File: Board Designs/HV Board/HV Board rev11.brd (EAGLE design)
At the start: 119.1 x 71.4 mm, 73 parts, among them IC1 OKI-78SR-5, IC2 NE5532SOIC

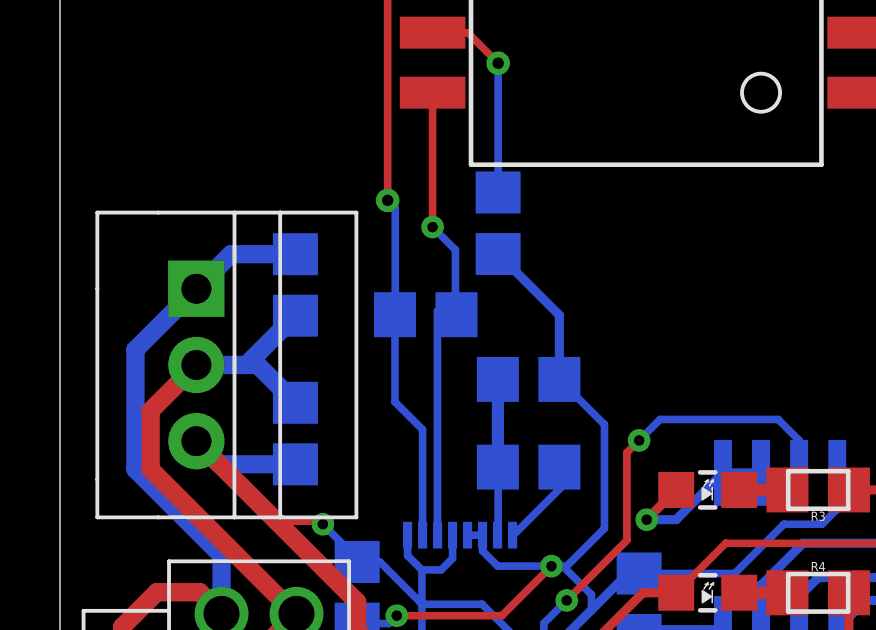
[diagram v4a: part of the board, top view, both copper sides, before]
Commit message: HV Board rev11: comp hardware - removed extra isoSPI resistor, changed LED resistor value
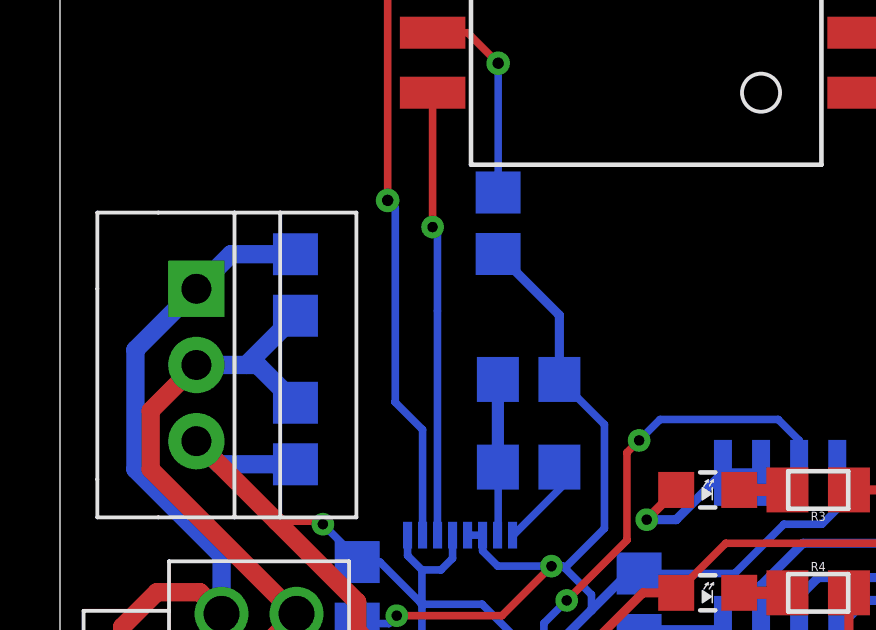
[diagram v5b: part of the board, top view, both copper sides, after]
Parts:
- removed R35: 120, HyTechDevices:0805
- R4: value 5k -> 2k
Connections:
- net IM: no longer R35.1
- net IP: no longer R35.2
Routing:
- net IP: track 15.9 -> 14.8 mm
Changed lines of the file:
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@@
 <layer number="18" name="Vias" color="2" fill="1" visible="yes" active="yes"/>
 <layer number="19" name="Unrouted" color="6" fill="1" visible="yes" active="yes"/>
-<layer number="20" name="Dimension" color="15" fill="1" visible="yes" active="yes"/>
+<layer number="20" name="Dimension" color="14" fill="1" visible="yes" active="yes"/>
 <layer number="21" name="tPlace" color="7" fill="1" visible="yes" active="yes"/>
 <layer number="22" name="bPlace" color="7" fill="1" visible="yes" active="yes"/>
@@
 <circle x="6.4008" y="23.6728" radius="3" width="0.127" layer="40"/>
 <circle x="32.3088" y="50.3428" radius="3" width="0.127" layer="40"/>
+<dimension x1="0" y1="71.374" x2="119.126" y2="71.374" x3="59.563" y3="73.406" textsize="1.778" layer="20"/>
+<dimension x1="0" y1="0" x2="0" y2="71.374" x3="-2.286" y3="35.687" textsize="1.778" layer="20"/>
 </plain>
 <attributes>
@@
 <attribute name="VALUE" x="28.702" y="45.4152" size="0.889" layer="27" font="vector" rot="R180" align="center"/>
 </element>
-<element name="R4" library="HyTechDevices" package="0805" value="5k" x="25.273" y="42.037" smashed="yes">
+<element name="R4" library="HyTechDevices" package="0805" value="2k" x="25.273" y="42.037" smashed="yes">
 <attribute name="NAME" x="25.273" y="42.7609" size="0.3048" layer="25" align="bottom-center"/>
 <attribute name="VALUE" x="28.194" y="42.0878" size="0.889" layer="27" font="vector" align="center"/>
@@
 <attribute name="VALUE" x="15.621" y="50.6222" size="0.889" layer="28" font="vector" rot="MR180" align="center"/>
 </element>
-<element name="R35" library="HyTechDevices" package="0805" value="120" x="12.192" y="51.308" smashed="yes" rot="MR180">
-<attribute name="NAME" x="12.192" y="50.5841" size="0.3048" layer="26" rot="MR180" align="bottom-center"/>
-<attribute name="VALUE" x="12.192" y="52.7812" size="0.889" layer="28" font="vector" rot="MR180" align="center"/>
-</element>
 <element name="C4" library="HyTechDevices" package="0805" value="27pF" x="14.605" y="54.356" smashed="yes" rot="MR270">
 <attribute name="NAME" x="14.3891" y="53.848" size="0.3048" layer="26" rot="MR270" align="bottom-center"/>
@@
 <signal name="IM">
 <contactref element="U$8" pad="10"/>
-<contactref element="R35" pad="1"/>
 <contactref element="U$2" pad="P$10"/>
 <wire x1="10.922" y1="62.357" x2="10.922" y2="55.118" width="0.254" layer="1"/>
-<wire x1="11.176" y1="54.864" x2="11.176" y2="51.317" width="0.254" layer="16"/>
-<wire x1="11.167" y1="51.308" x2="11.176" y2="51.317" width="0.254" layer="16"/>
-<wire x1="11.176" y1="54.864" x2="10.922" y2="55.118" width="0.254" layer="16"/>
+<wire x1="10.922" y1="55.118" x2="11.176" y2="54.864" width="0.254" layer="16"/>
 <via x="10.922" y="55.118" extent="1-16" drill="0.381"/>
 <wire x1="12.42" y1="62.707" x2="11.272" y2="62.707" width="0.254" layer="1"/>
 <wire x1="11.272" y1="62.707" x2="10.922" y2="62.357" width="0.254" layer="1"/>
-<wire x1="12.086" y1="47.477" x2="11.167" y2="48.396" width="0.254" layer="16"/>
-<wire x1="11.167" y1="51.308" x2="11.167" y2="48.396" width="0.254" layer="16"/>
+<wire x1="11.167" y1="48.396" x2="12.086" y2="47.477" width="0.254" layer="16"/>
 <wire x1="12.086" y1="47.477" x2="12.086" y2="43.959" width="0.254" layer="16"/>
+<wire x1="11.176" y1="48.405" x2="11.167" y2="48.396" width="0.254" layer="16"/>
+<wire x1="11.176" y1="54.864" x2="11.176" y2="48.405" width="0.254" layer="16"/>
 </signal>
 <signal name="IP">
 <contactref element="U$8" pad="11"/>
-<contactref element="R35" pad="2"/>
 <contactref element="U$2" pad="P$12"/>
-<wire x1="13.217" y1="51.308" x2="13.182" y2="51.308" width="0.254" layer="16"/>
 <via x="12.42" y="54.229" extent="1-16" drill="0.35"/>
 <wire x1="12.42" y1="58.707" x2="12.42" y2="54.229" width="0.254" layer="1"/>
-<wire x1="12.42" y1="54.229" x2="13.182" y2="53.467" width="0.254" layer="16"/>
-<wire x1="13.182" y1="53.467" x2="13.182" y2="51.308" width="0.254" layer="16"/>
-<wire x1="13.217" y1="51.308" x2="12.709" y2="51.308" width="0.254" layer="16"/>
-<wire x1="12.709" y1="51.308" x2="12.582" y2="51.435" width="0.254" layer="16"/>
 <wire x1="12.582" y1="51.435" x2="12.582" y2="43.963" width="0.254" layer="16"/>
 <wire x1="12.582" y1="43.963" x2="12.586" y2="43.959" width="0.254" layer="16"/>
+<wire x1="12.582" y1="51.435" x2="12.582" y2="54.067" width="0.254" layer="16"/>
+<wire x1="12.582" y1="54.067" x2="12.42" y2="54.229" width="0.254" layer="16"/>
 </signal>
 <signal name="ISOSPI-P" class="2">
